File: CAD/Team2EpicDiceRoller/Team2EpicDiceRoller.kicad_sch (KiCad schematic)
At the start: 68 parts, among them J1 Conn_02x03_Odd_Even, J2 Conn_01x16, J3 Barrel_Jack, Q1 BSS138, SW1 SW_Toggle_SPDT, SW2 Tilt_Switch, SW3 SW_Power, SW4 RotaryEncoder_Switch, SW5 SW_LeftMenu, SW6 SW_MidMenu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

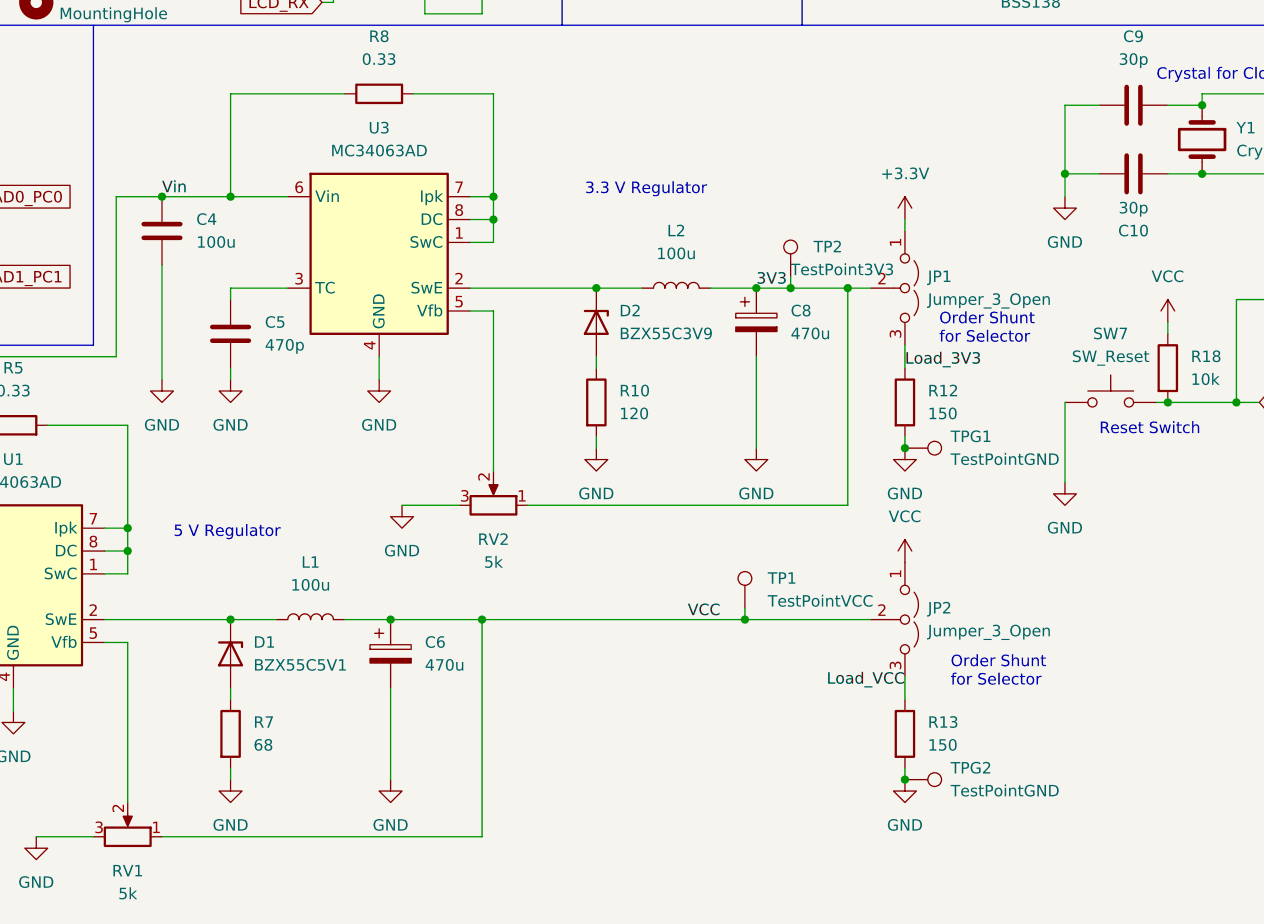
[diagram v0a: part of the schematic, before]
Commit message: Added cap, moved pots, many changes
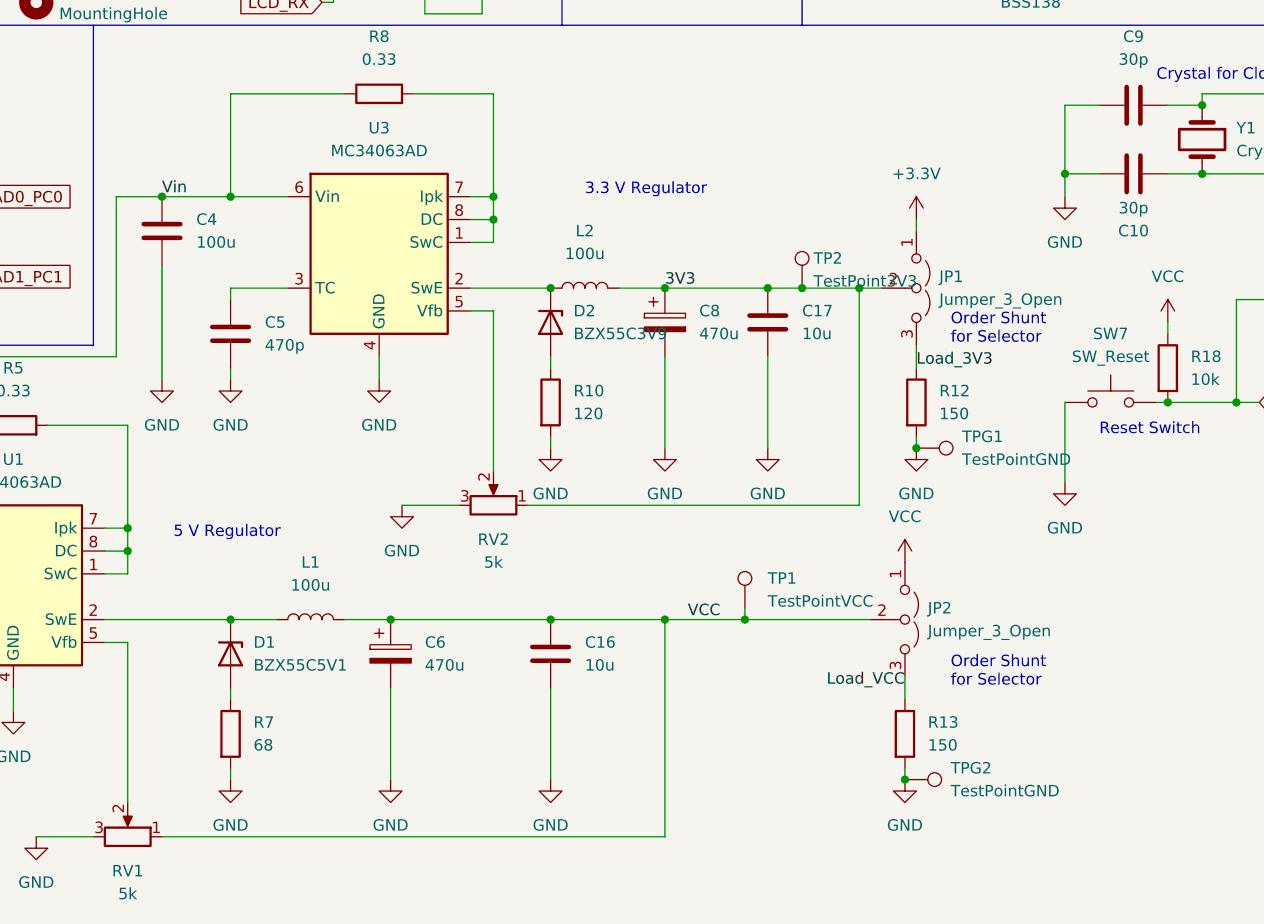
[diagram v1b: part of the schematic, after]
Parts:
- added C16, C17: 10u, Capacitor_SMD:C_1206_3216Metric_Pad1.33x1.80mm_HandSolder, symbol Device:C
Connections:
- net 3V3: now also C17.1
- net GND: now also C16.2, C17.2
- net VCC: now also C16.1
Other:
- moved on the sheet: C8, D2, JP1, L2, R10, R12, TP2, TPG1

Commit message: Updated silk screen, ready to route
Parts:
- added H1, H2: MountingHole, MountingHole:MountingHole_3.2mm_M3, symbol Mechanical:MountingHole
- renumbered H1 to H3, H2 to H4
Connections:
- net IO2_PD2: now also R22.1; no longer R21.2
- net IO3_PD3: now also R21.2; no longer R22.1
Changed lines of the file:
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@@
   )
   (text "Female Header for 16x2 LCD Screen\nSparkfun RGB LCD Screen"
-    (at 68.58 76.2 0)
+    (at 68.58 74.93 0)
     (effects (font (size 1.27 1.27)) (justify left bottom))
   )
@@
     (effects (font (size 1.27 1.27)) (justify left bottom))
   )
-  (global_label "IO2_PD2" (shape output) (at 19.05 22.86 90) (fields_autoplaced)
+  (global_label "IO3_PD3" (shape output) (at 19.05 22.86 90) (fields_autoplaced)
     (effects (font (size 1.27 1.27)) (justify left))
     (property "Intersheet References" "${INTERSHEET_REFS}" (id 0) (at 19.1294 12.585 90)
@@
     )
   )
-  (global_label "IO3_PD3" (shape output) (at 26.67 45.72 0) (fields_autoplaced)
+  (global_label "IO2_PD2" (shape output) (at 26.67 45.72 0) (fields_autoplaced)
     (effects (font (size 1.27 1.27)) (justify left))
     (property "Intersheet References" "${INTERSHEET_REFS}" (id 0) (at 36.945 45.7994 0)
@@
     (pin "2")
   )
+  (symbol (lib_id "Mechanical:MountingHole") (at 58.42 74.93 0) (unit 1)
+    (in_bom yes) (on_board yes) (fields_autoplaced)
+    (property "Reference" "H1" (id 0) (at 60.96 73.6599 0)
+      (effects (font (size 1.27 1.27)) (justify left))
+    )
+    (property "Value" "MountingHole" (id 1) (at 60.96 76.1999 0)
+      (effects (font (size 1.27 1.27)) (justify left))
+    )
+    (property "Footprint" "MountingHole:MountingHole_3.2mm_M3" (id 2) (at 58.42 74.93 0)
+      (effects (font (size 1.27 1.27)) hide)
+    )
+    (property "Datasheet" "~" (id 3) (at 58.42 74.93 0)
+      (effects (font (size 1.27 1.27)) hide)
+    )
+  )
+  (symbol (lib_id "Mechanical:MountingHole") (at 58.42 80.01 0) (unit 1)
+    (in_bom yes) (on_board yes) (fields_autoplaced)
+    (property "Reference" "H2" (id 0) (at 60.96 78.7399 0)
+      (effects (font (size 1.27 1.27)) (justify left))
+    )
+    (property "Value" "MountingHole" (id 1) (at 60.96 81.2799 0)
+      (effects (font (size 1.27 1.27)) (justify left))
+    )
+    (property "Footprint" "MountingHole:MountingHole_3.2mm_M3" (id 2) (at 58.42 80.01 0)
+      (effects (font (size 1.27 1.27)) hide)
+    )
+    (property "Datasheet" "~" (id 3) (at 58.42 80.01 0)
+      (effects (font (size 1.27 1.27)) hide)
+    )
+  )
   (symbol (lib_id "Mechanical:MountingHole") (at 58.42 92.71 0) (unit 1)
     (in_bom yes) (on_board yes) (fields_autoplaced)
-    (property "Reference" "H1" (id 0) (at 60.96 91.4399 0)
+    (property "Reference" "H3" (id 0) (at 60.96 91.4399 0)
       (effects (font (size 1.27 1.27)) (justify left))
     )
@@
   (symbol (lib_id "Mechanical:MountingHole") (at 58.42 97.79 0) (unit 1)
     (in_bom yes) (on_board yes) (fields_autoplaced)
-    (property "Reference" "H2" (id 0) (at 60.96 96.5199 0)
+    (property "Reference" "H4" (id 0) (at 60.96 96.5199 0)
       (effects (font (size 1.27 1.27)) (justify left))
     )
@@
       (reference "D2") (unit 1) (value "BZX55C3V9") (footprint "Diode_THT:D_DO-35_SOD27_P7.62mm_Horizontal")
     )
+    (path "/8df55893-6d5c-42a6-88f4-d8d86fb6ee12"
+      (reference "H1") (unit 1) (value "MountingHole") (footprint "MountingHole:MountingHole_3.2mm_M3")
+    )
+    (path "/0bca1254-8920-4ff0-a882-771ba6139615"
+      (reference "H2") (unit 1) (value "MountingHole") (footprint "MountingHole:MountingHole_3.2mm_M3")
+    )
     (path "/89d096c1-e2f8-495f-b214-91c56d1cbee4"
-      (reference "H1") (unit 1) (value "MountingHole") (footprint "MountingHole:MountingHole_3.2mm_M3")
+      (reference "H3") (unit 1) (value "MountingHole") (footprint "MountingHole:MountingHole_3.2mm_M3")
     )
     (path "/f32266d9-a3df-4950-8cf5-205f2086c5fb"
-      (reference "H2") (unit 1) (value "MountingHole") (footprint "MountingHole:MountingHole_3.2mm_M3")
+      (reference "H4") (unit 1) (value "MountingHole") (footprint "MountingHole:MountingHole_3.2mm_M3")
     )
     (path "/97500fde-4c78-42dd-ab07-3c6ad623f25a"

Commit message: Stephens first route
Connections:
- net IO10_SS_PB2: now also U2.8
- net IO4_PD4: no longer U2.8
- net VCC: no longer C16.1, C6.1, JP2.2 (C), L1.2, RV1.1, TP1.1
- new net: C16.1, C6.1, JP2.2 (C), L1.2, RV1.1, TP1.1
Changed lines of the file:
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@@
-    (effects (font (size 1.27 1.27)) (justify left bottom))
-  )
-  (label "VCC" (at 130.81 166.37 0)
     (effects (font (size 1.27 1.27)) (justify left bottom))
   )
@@
     )
   )
-  (global_label "IO4_PD4" (shape output) (at 90.17 30.48 0) (fields_autoplaced)
-    (effects (font (size 1.27 1.27)) (justify left))
-    (property "Intersheet References" "${INTERSHEET_REFS}" (id 0) (at 100.445 30.4006 0)
+  (global_label "IO10_SS_PB2" (shape input) (at 90.17 30.48 270) (fields_autoplaced)
+    (effects (font (size 1.27 1.27)) (justify right))
+    (property "Intersheet References" "${INTERSHEET_REFS}" (id 0) (at 90.2494 45.3512 90)
       (effects (font (size 1.27 1.27)) (justify left) hide)
     )
